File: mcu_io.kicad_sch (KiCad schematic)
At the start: 10 parts, among them U3 SiWG917Y, U9 PCAL6408AHK

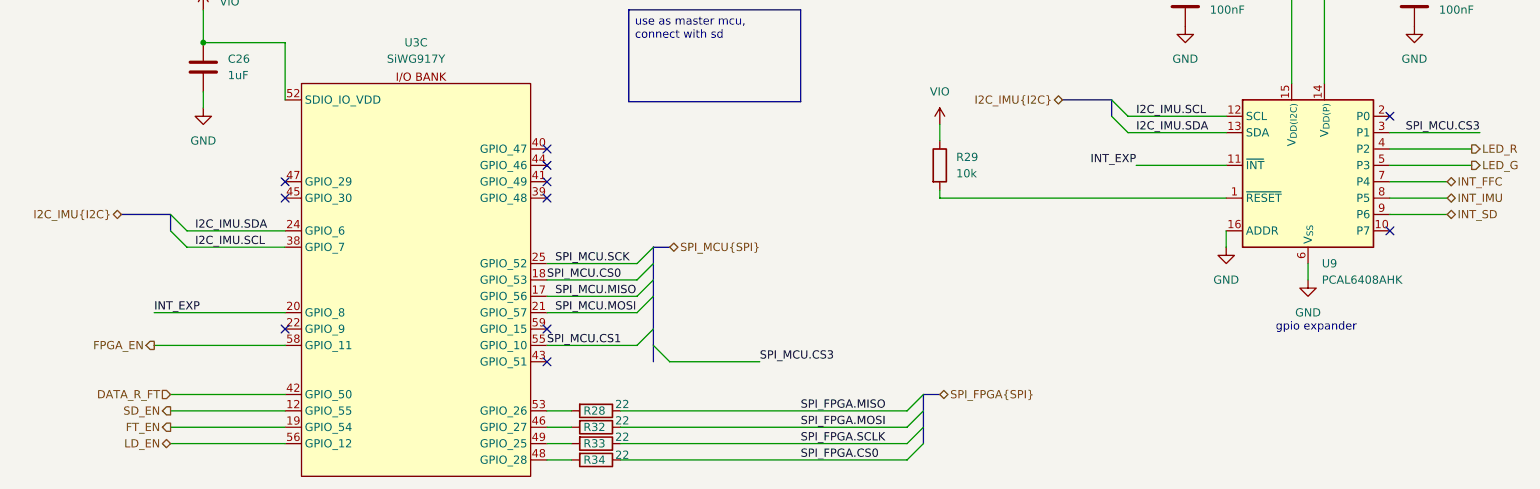
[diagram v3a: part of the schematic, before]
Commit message: updated schematic and initial pcb placement
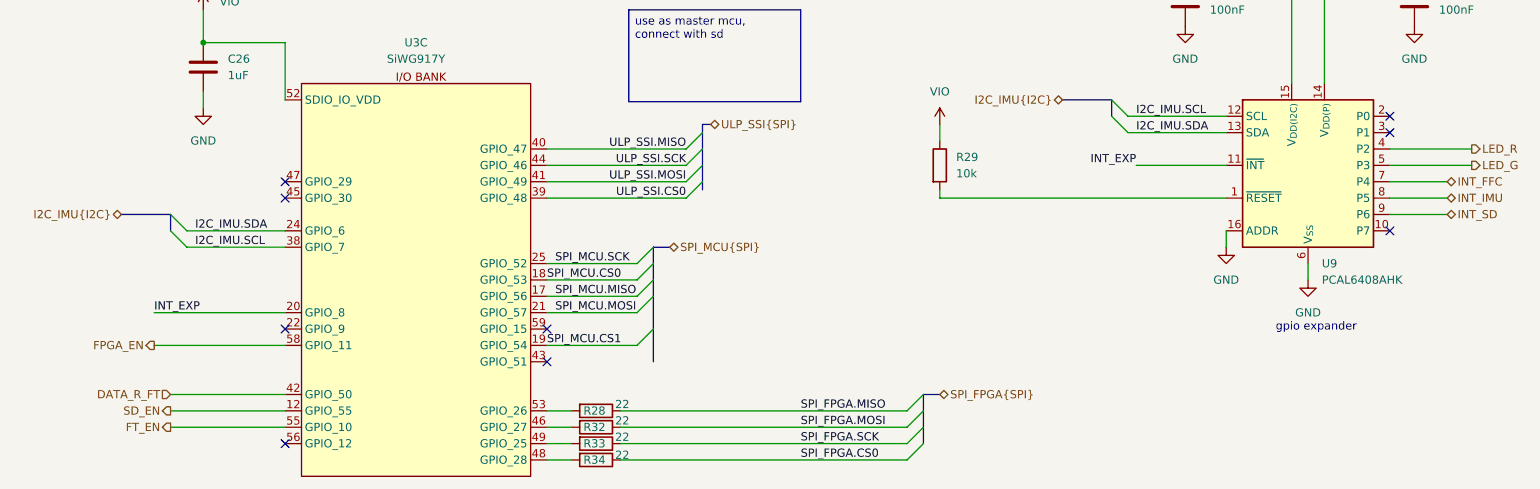
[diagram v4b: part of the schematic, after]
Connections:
- net FT_EN: now also U3.55 (GPIO_10); no longer U3.19 (GPIO_54)
- net SPI_MCU.CS1: now also U3.19 (GPIO_54); no longer U3.55 (GPIO_10)
- net ULP_SSI.CS0: now reaches U3.39 (GPIO_48)
- net ULP_SSI.MISO: now reaches U3.40 (GPIO_47)
- net ULP_SSI.MOSI: now reaches U3.41 (GPIO_49)
- net ULP_SSI.SCK: now reaches U3.44 (GPIO_46)
- net LD_EN: no longer names the net of U3.56 (GPIO_12)
- net SPI_FPGA.SCLK renamed SPI_FPGA.SCK
- net SPI_MCU.CS3: no longer names the net of U9.3 (P1)
- no-connect marks 11 -> 9
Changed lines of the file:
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@@
 	)
 	(no_connect
-		(at 96.52 71.12)
-	)
-	(no_connect
-		(at 96.52 68.58)
+		(at 55.88 114.3)
 	)
 	(no_connect
@@
 	)
 	(no_connect
+		(at 227.33 66.04)
+	)
+	(no_connect
 		(at 55.88 76.2)
 	)
@@
 	)
 	(no_connect
-		(at 96.52 73.66)
-	)
-	(no_connect
 		(at 227.33 63.5)
-	)
-	(no_connect
-		(at 96.52 76.2)
 	)
 	(no_connect
@@
 	)
 	(bus_entry
+		(at 118.11 68.58)
+		(size 2.54 -2.54)
+		(stroke
+			(width 0)
+			(type default)
+		)
+	)
+	(bus_entry
 		(at 38.1 81.28)
 		(size 2.54 2.54)
@@
 	)
 	(bus_entry
+		(at 118.11 73.66)
+		(size 2.54 -2.54)
+		(stroke
+			(width 0)
+			(type default)
+		)
+	)
+	(bus_entry
+		(at 118.11 76.2)
+		(size 2.54 -2.54)
+		(stroke
+			(width 0)
+			(type default)
+		)
+	)
+	(bus_entry
 		(at 113.03 91.44)
 		(size -2.54 2.54)
@@
 	)
 	(bus_entry
-		(at 113.03 99.06)
-		(size 2.54 2.54)
+		(at 118.11 71.12)
+		(size 2.54 -2.54)
 		(stroke
 			(width 0)
@@
 	(wire
 		(pts
+			(xy 96.52 68.58) (xy 118.11 68.58)
+		)
+		(stroke
+			(width 0)
+			(type default)
+		)
+	)
+	(wire
+		(pts
 			(xy 96.52 109.22) (xy 100.33 109.22)
 		)
@@
 	(wire
 		(pts
-			(xy 38.1 114.3) (xy 55.88 114.3)
-		)
-		(stroke
-			(width 0)
-			(type default)
-		)
-	)
-	(wire
-		(pts
 			(xy 201.93 76.2) (xy 157.48 76.2)
 		)
@@
 	(bus
 		(pts
+			(xy 121.92 64.77) (xy 120.65 64.77)
+		)
+		(stroke
+			(width 0)
+			(type default)
+		)
+	)
+	(bus
+		(pts
 			(xy 38.1 78.74) (xy 30.48 78.74)
 		)
@@
 		)
 	)
+	(bus
+		(pts
+			(xy 120.65 74.93) (xy 120.65 64.77)
+		)
+		(stroke
+			(width 0)
+			(type default)
+		)
+	)
 	(wire
 		(pts
@@
 	(wire
 		(pts
-			(xy 129.54 101.6) (xy 115.57 101.6)
-		)
-		(stroke
-			(width 0)
-			(type default)
-		)
-	)
-	(wire
-		(pts
-			(xy 241.3 66.04) (xy 227.33 66.04)
-		)
-		(stroke
-			(width 0)
-			(type default)
-		)
-	)
-	(wire
-		(pts
 			(xy 231.14 35.56) (xy 231.14 41.91)
 		)
@@
 	(wire
 		(pts
+			(xy 118.11 73.66) (xy 96.52 73.66)
+		)
+		(stroke
+			(width 0)
+			(type default)
+		)
+	)
+	(wire
+		(pts
 			(xy 40.64 83.82) (xy 55.88 83.82)
 		)
@@
 	(wire
 		(pts
+			(xy 96.52 76.2) (xy 118.11 76.2)
+		)
+		(stroke
+			(width 0)
+			(type default)
+		)
+	)
+	(wire
+		(pts
 			(xy 96.52 91.44) (xy 110.49 91.44)
 		)
@@
 		)
 	)
-	(label "SPI_MCU.CS3"
-		(at 129.54 101.6 0)
-		(effects
-			(font
-				(size 1.27 1.27)
-			)
-			(justify left bottom)
+	(wire
+		(pts
+			(xy 118.11 71.12) (xy 96.52 71.12)
+		)
+		(stroke
+			(width 0)
+			(type default)
 		)
 	)
@@
 		)
 	)
-	(label "SPI_FPGA.SCLK"
+	(label "SPI_FPGA.SCK"
 		(at 135.89 114.3 0)
 		(effects
@@
 		)
 	)
+	(label "ULP_SSI.MOSI"
+		(at 118.11 73.66 180)
+		(effects
+			(font
+				(size 1.27 1.27)
+			)
+			(justify right bottom)
+		)
+	)
+	(label "ULP_SSI.SCK"
+		(at 118.11 71.12 180)
+		(effects
+			(font
+				(size 1.27 1.27)
+			)
+			(justify right bottom)
+		)
+	)
 	(label "SPI_MCU.MISO"
 		(at 97.79 91.44 0)
@@
 		)
 	)
+	(label "ULP_SSI.MISO"
+		(at 118.11 68.58 180)
+		(effects
+			(font
+				(size 1.27 1.27)
+			)
+			(justify right bottom)
+		)
+	)
 	(label "SPI_FPGA.MOSI"
 		(at 135.89 111.76 0)
@@
 		)
 	)
-	(label "SPI_MCU.CS3"
-		(at 241.3 66.04 180)
-		(effects
-			(font
-				(size 1.27 1.27)
-			)
-			(justify right bottom)
-		)
-	)
 	(label "SPI_FPGA.MISO"
 		(at 135.89 109.22 0)
@@
 			)
 			(justify left bottom)
+		)
+	)
+	(label "ULP_SSI.CS0"
+		(at 118.11 76.2 180)
+		(effects
+			(font
+				(size 1.27 1.27)
+			)
+			(justify right bottom)
 		)
 	)
@@
 		)
 	)
-	(hierarchical_label "LD_EN"
-		(shape bidirectional)
-		(at 38.1 114.3 180)
-		(effects
-			(font
-				(size 1.27 1.27)
-			)
-			(justify right)
-		)
-	)
 	(hierarchical_label "INT_FFC"
 		(shape bidirectional)
@@
 		(effects
 			(font
+				(size 1.27 1.27)
+			)
+			(justify left)
+		)
+	)
+	(hierarchical_label "ULP_SSI{SPI}"
+		(shape bidirectional)
+		(at 121.92 64.77 0)
+		(effects
+			(font
